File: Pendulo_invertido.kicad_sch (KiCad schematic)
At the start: 9 parts, among them IC2 MPU-6050, J3 Conn_01x02, J4 Conn_01x02, J5 Conn_01x02, U1 ESP32-devkitc, U2 TB6612FNG, U3 LM7805_TO220

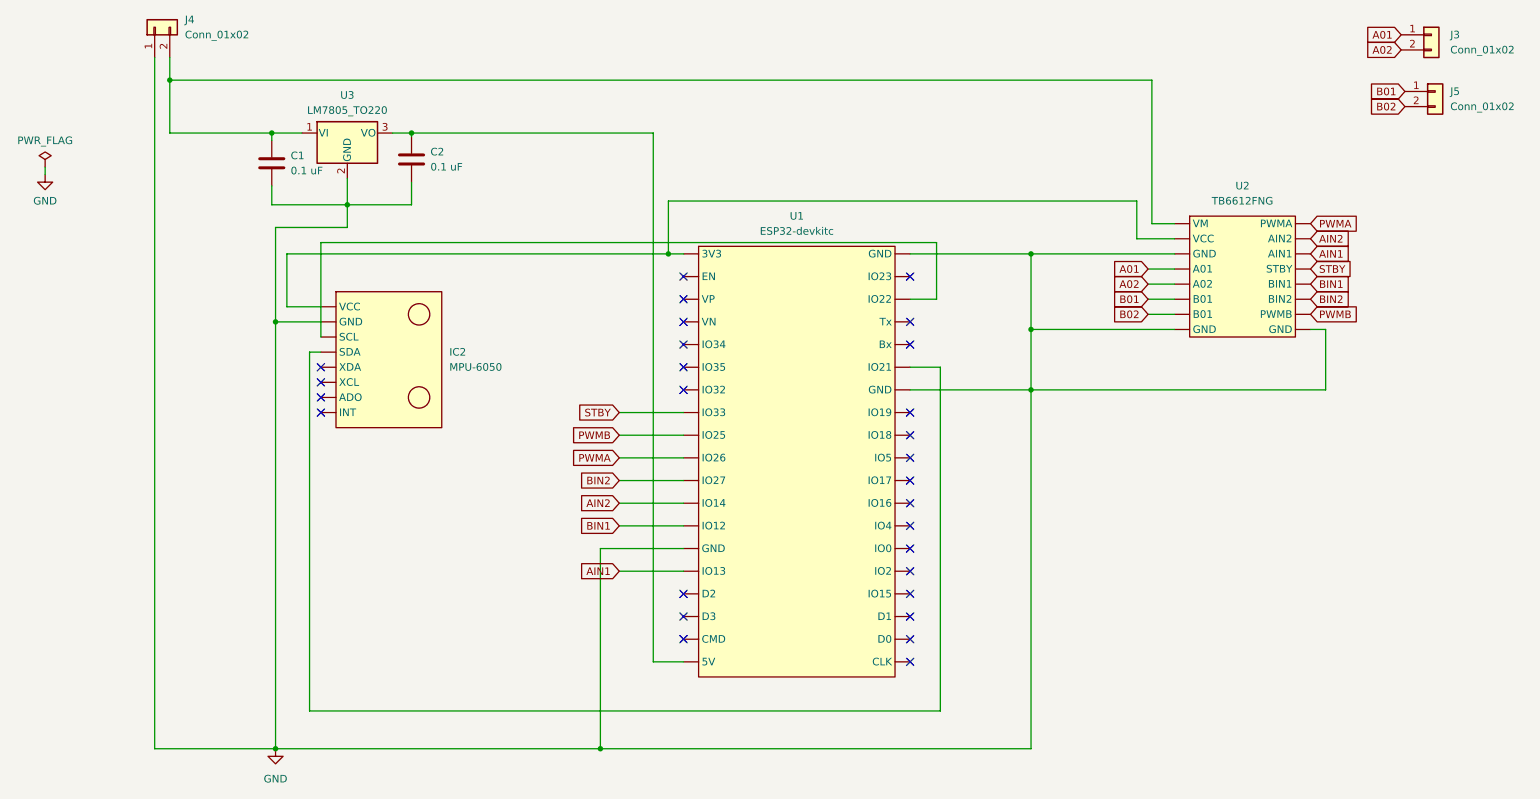
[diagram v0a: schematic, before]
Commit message: Creacion huellas esp32 y MPU
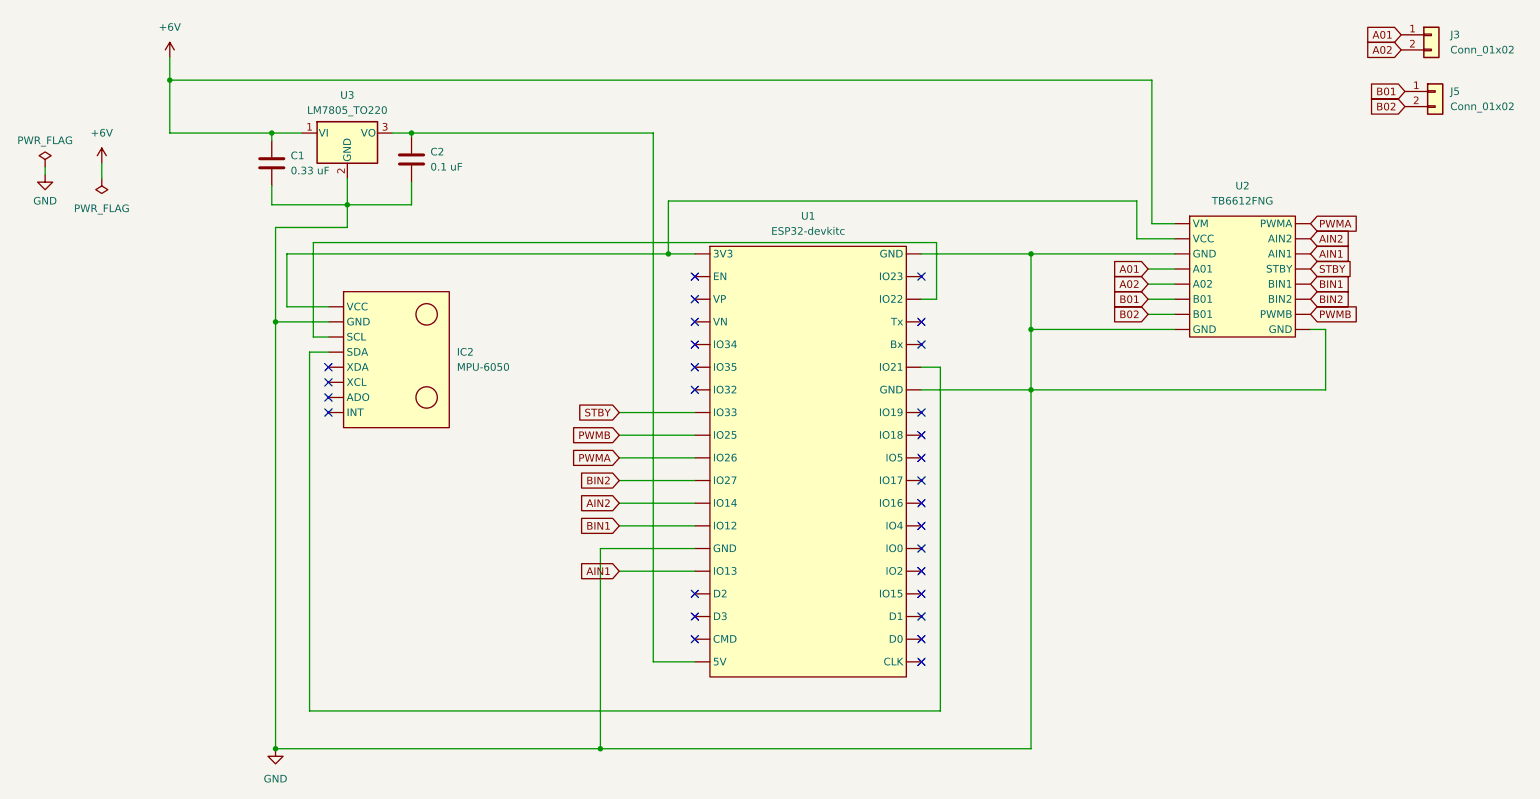
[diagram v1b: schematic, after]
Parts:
- removed J4: Conn_01x02, symbol Connector_Generic:Conn_01x02
- C1: value 0.1 uF -> 0.33 uF; footprint (none) -> Capacitor_THT:CP_Radial_D5.0mm_P2.00mm
- C2: footprint (none) -> Capacitor_THT:CP_Radial_D5.0mm_P2.00mm
- J3, J5: footprint (none) -> Connector_JST:JST_XH_B2B-XH-A_1x02_P2.50mm_Vertical
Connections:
- net +6V: now reaches C1.1, U2. (VM), U3.1 (VI)
- new net: IC2. (XDA), U1. (VP), U2. (VM)
- new net: IC2. (XDA), U1. (VP) (x2)
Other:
- moved on the sheet: IC2

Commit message: Creación pcb
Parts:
- removed IC2: MPU-6050, symbol New_Library:MPU-6050
- added IC1: MPU-6050, symbol New_Library:MPU-6050
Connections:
- net +6V: now also U2.1 (VM); no longer U2. (VM)
- net A01: now also U2.4 (A01); no longer U2. (VM)
- net A02: now also U2.5 (A02); no longer U2. (VM)
- net AIN1: now also U1.15 (IO13), U2.14 (AIN1); no longer U1. (VP), U2. (VM)
- net AIN2: now also U1.12 (IO14), U2.15 (AIN2); no longer U1. (VP), U2. (VM)
- net B01: now also U2.6 (B01); no longer U2. (VM)
- net B02: now also U2.7 (B01); no longer U2. (VM)
- net BIN1: now also U1.13 (IO12), U2.12 (BIN1); no longer U1. (VP), U2. (VM)
- net BIN2: now also U1.11 (IO27), U2.11 (BIN2); no longer U1. (VP), U2. (VM)
- net GND: now also U1.14 (GND), U1.32 (GND), U1.38 (GND), U2.3 (GND), U2.8 (GND), U2.9 (GND), IC1.2 (GND); no longer U1. (VP), U2. (VM)
- net PWMA: now also U1.10 (IO26), U2.16 (PWMA); no longer U1. (VP), U2. (VM)
- net PWMB: now also U1.9 (IO25), U2.10 (PWMB); no longer U1. (VP), U2. (VM)
- net STBY: now also U1.8 (IO33), U2.13 (STBY); no longer U1. (VP), U2. (VM)
- net at C2.1, U3.3 (VO): now also U1.19 (5V); no longer U1. (VP)
- new net: IC1.1 (VCC), U1.1 (3V3), U2.2 (VCC)
- new net: IC1.4 (SDA), U1.33 (IO21)
- new net: IC1.3 (SCL), U1.36 (IO22)

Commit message: Cambios huellas y pcb
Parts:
- added J1: Conn_01x02, TerminalBlock_Phoenix:TerminalBlock_Phoenix_MKDS-1,5-2-5.08_1x02_P5.08mm_Horizontal, symbol Connector_Generic:Conn_01x02
- IC1: footprint (none) -> Library:MPU6050
- J3, J5: footprint Connector_JST:JST_XH_B2B-XH-A_1x02_P2.50mm_Vertical -> TerminalBlock_Phoenix:TerminalBlock_Phoenix_MKDS-1,5-2-5.08_1x02_P5.08mm_Horizontal
- U1: footprint (none) -> Library:ESP32-devkitc-v4
- U2: footprint (none) -> Library:TB6612FNG
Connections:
- net +6V: now also J1.2 (Pin_2)
- net GND: now also J1.1 (Pin_1)
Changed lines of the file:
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@@
 (kicad_sch (version 20230121) (generator eeschema)
   (paper "A4")
+  (junction (at 49.53 36.83) (diameter 0) (color 0 0 0 0)
+  )
   (junction (at 66.675 45.72) (diameter 0) (color 0 0 0 0)
   )
+  (junction (at 49.53 33.02) (diameter 0) (color 0 0 0 0)
+  )
   (junction (at 133.35 66.04) (diameter 0) (color 0 0 0 0)
   )
   (junction (at 67.31 77.47) (diameter 0) (color 0 0 0 0)
-  )
-  (junction (at 49.53 36.83) (diameter 0) (color 0 0 0 0)
   )
   (junction (at 79.375 57.785) (diameter 0) (color 0 0 0 0)
@@
   (no_connect (at 177.165 130.81))
   (no_connect (at 177.165 104.14))
+  (wire (pts (xy 46.99 33.02) (xy 46.99 149.225))
+    (stroke (width 0) (type default))
+  )
   (wire (pts (xy 243.84 88.9) (xy 194.31 88.9))
     (stroke (width 0) (type default))
@@
     (stroke (width 0) (type default))
   )
+  (wire (pts (xy 67.945 33.02) (xy 67.945 32.385))
+    (stroke (width 0) (type default))
+  )
   (wire (pts (xy 213.995 76.2) (xy 218.44 76.2))
     (stroke (width 0) (type default))
@@
     (stroke (width 0) (type default))
   )
+  (wire (pts (xy 46.99 149.225) (xy 67.31 149.225))
+    (stroke (width 0) (type default))
+  )
   (wire (pts (xy 194.31 149.225) (xy 121.92 149.225))
     (stroke (width 0) (type default))
@@
     (stroke (width 0) (type default))
   )
+  (wire (pts (xy 49.53 33.02) (xy 67.945 33.02))
+    (stroke (width 0) (type default))
+  )
   (wire (pts (xy 177.165 88.9) (xy 194.31 88.9))
     (stroke (width 0) (type default))
@@
     (stroke (width 0) (type default))
   )
+  (wire (pts (xy 49.53 33.02) (xy 49.53 36.83))
+    (stroke (width 0) (type default))
+  )
   (wire (pts (xy 73.025 142.875) (xy 73.025 82.55))
     (stroke (width 0) (type default))
@@
   )
   (wire (pts (xy 212.09 63.5) (xy 212.09 57.15))
-    (stroke (width 0) (type default))
-  )
-  (wire (pts (xy 49.53 33.02) (xy 49.53 36.83))
     (stroke (width 0) (type default))
   )
@@
       (effects (font (size 1.27 1.27)))
     )
-    (property "Footprint" "" (at 146.685 64.77 0)
+    (property "Footprint" "Library:ESP32-devkitc-v4" (at 146.685 64.77 0)
       (effects (font (size 1.27 1.27)) hide)
     )
@@
       (effects (font (size 1.27 1.27)) (justify left))
     )
-    (property "Footprint" "Connector_JST:JST_XH_B2B-XH-A_1x02_P2.50mm_Vertical" (at 261.62 29.21 0)
+    (property "Footprint" "TerminalBlock_Phoenix:TerminalBlock_Phoenix_MKDS-1,5-2-5.08_1x02_P5.08mm_Horizontal" (at 261.62 29.21 0)
       (effects (font (size 1.27 1.27)) hide)
     )
@@
       (effects (font (size 1.27 1.27)))
     )
-    (property "Footprint" "" (at 226.06 58.42 0)
+    (property "Footprint" "Library:TB6612FNG" (at 226.06 58.42 0)
       (effects (font (size 1.27 1.27)) hide)
     )
@@
     )
   )
+  (symbol (lib_id "Connector_Generic:Conn_01x02") (at 46.99 27.94 90) (unit 1)
+    (in_bom yes) (on_board yes) (dnp no) (fields_autoplaced)
+    (property "Reference" "J1" (at 52.07 26.67 90)
+      (effects (font (size 1.27 1.27)) (justify right))
+    )
+    (property "Value" "Conn_01x02" (at 52.07 29.21 90)
+      (effects (font (size 1.27 1.27)) (justify right))
+    )
+    (property "Footprint" "TerminalBlock_Phoenix:TerminalBlock_Phoenix_MKDS-1,5-2-5.08_1x02_P5.08mm_Horizontal" (at 46.99 27.94 0)
+      (effects (font (size 1.27 1.27)) hide)
+    )
+    (property "Datasheet" "~" (at 46.99 27.94 0)
+      (effects (font (size 1.27 1.27)) hide)
+    )
+    (pin "1")
+    (pin "2")
+    (instances
+      (project "Pendulo_invertido"
+        (path "/1d6a1010-cae9-4f43-acf9-dddad0fedfc5"
+          (reference "J1") (unit 1)
+        )
+      )
+    )
+  )
   (symbol (lib_id "power:PWR_FLAG") (at 38.1 53.34 180) (unit 1)
     (in_bom yes) (on_board yes) (dnp no) (fields_autoplaced)
@@
     )
   )
-  (symbol (lib_id "power:+6V") (at 49.53 33.02 0) (unit 1)
-    (in_bom yes) (on_board yes) (dnp no) (fields_autoplaced)
-    (property "Reference" "#PWR03" (at 49.53 36.83 0)
-      (effects (font (size 1.27 1.27)) hide)
-    )
-    (property "Value" "+6V" (at 49.53 27.94 0)
-      (effects (font (size 1.27 1.27)))
-    )
-    (property "Footprint" "" (at 49.53 33.02 0)
-      (effects (font (size 1.27 1.27)) hide)
-    )
-    (property "Datasheet" "" (at 49.53 33.02 0)
+  (symbol (lib_id "power:GND") (at 28.575 52.705 0) (unit 1)
+    (in_bom yes) (on_board yes) (dnp no) (fields_autoplaced)
+    (property "Reference" "#PWR02" (at 28.575 59.055 0)
+      (effects (font (size 1.27 1.27)) hide)
+    )
+    (property "Value" "GND" (at 28.575 57.15 0)
+      (effects (font (size 1.27 1.27)))
+    )
+    (property "Footprint" "" (at 28.575 52.705 0)
+      (effects (font (size 1.27 1.27)) hide)
+    )
+    (property "Datasheet" "" (at 28.575 52.705 0)
+      (effects (font (size 1.27 1.27)) hide)
+    )
+    (pin "1")
+    (instances
+      (project "Pendulo_invertido"
+        (path "/1d6a1010-cae9-4f43-acf9-dddad0fedfc5"
+          (reference "#PWR02") (unit 1)
+        )
+      )
+    )
+  )
+  (symbol (lib_id "Connector_Generic:Conn_01x02") (at 262.255 38.735 0) (unit 1)
+    (in_bom yes) (on_board yes) (dnp no) (fields_autoplaced)
+    (property "Reference" "J5" (at 264.795 38.735 0)
+      (effects (font (size 1.27 1.27)) (justify left))
+    )
+    (property "Value" "Conn_01x02" (at 264.795 41.275 0)
+      (effects (font (size 1.27 1.27)) (justify left))
+    )
+    (property "Footprint" "TerminalBlock_Phoenix:TerminalBlock_Phoenix_MKDS-1,5-2-5.08_1x02_P5.08mm_Horizontal" (at 262.255 38.735 0)
+      (effects (font (size 1.27 1.27)) hide)
+    )
+    (property "Datasheet" "~" (at 262.255 38.735 0)
+      (effects (font (size 1.27 1.27)) hide)
+    )
+    (pin "1")
+    (pin "2")
+    (instances
+      (project "Pendulo_invertido"
+        (path "/1d6a1010-cae9-4f43-acf9-dddad0fedfc5"
+          (reference "J5") (unit 1)
+        )
+      )
+    )
+  )
+  (symbol (lib_id "Device:C") (at 90.17 50.165 0) (unit 1)
+    (in_bom yes) (on_board yes) (dnp no) (fields_autoplaced)
+    (property "Reference" "C2" (at 93.345 48.895 0)
+      (effects (font (size 1.27 1.27)) (justify left))
+    )
+    (property "Value" "0.1 uF" (at 93.345 51.435 0)
+      (effects (font (size 1.27 1.27)) (justify left))
+    )
+    (property "Footprint" "Capacitor_THT:CP_Radial_D5.0mm_P2.00mm" (at 91.1352 53.975 0)
+      (effects (font (size 1.27 1.27)) hide)
+    )
+    (property "Datasheet" "~" (at 90.17 50.165 0)
+      (effects (font (size 1.27 1.27)) hide)
+    )
+    (pin "1")
+    (pin "2")
+    (instances
+      (project "Pendulo_invertido"
+        (path "/1d6a1010-cae9-4f43-acf9-dddad0fedfc5"
+          (reference "C2") (unit 1)
+        )
+      )
+    )
+  )
+  (symbol (lib_id "power:+6V") (at 67.945 32.385 0) (unit 1)
+    (in_bom yes) (on_board yes) (dnp no) (fields_autoplaced)
+    (property "Reference" "#PWR03" (at 67.945 36.195 0)
+      (effects (font (size 1.27 1.27)) hide)
+    )
+    (property "Value" "+6V" (at 67.945 27.94 0)
+      (effects (font (size 1.27 1.27)))
+    )
+    (property "Footprint" "" (at 67.945 32.385 0)
+      (effects (font (size 1.27 1.27)) hide)
+    )
+    (property "Datasheet" "" (at 67.945 32.385 0)
       (effects (font (size 1.27 1.27)) hide)
     )
@@
     )
   )
-  (symbol (lib_id "power:GND") (at 28.575 52.705 0) (unit 1)
-    (in_bom yes) (on_board yes) (dnp no) (fields_autoplaced)
-    (property "Reference" "#PWR02" (at 28.575 59.055 0)
-      (effects (font (size 1.27 1.27)) hide)
-    )
-    (property "Value" "GND" (at 28.575 57.15 0)
-      (effects (font (size 1.27 1.27)))
-    )
-    (property "Footprint" "" (at 28.575 52.705 0)
-      (effects (font (size 1.27 1.27)) hide)
-    )
-    (property "Datasheet" "" (at 28.575 52.705 0)
-      (effects (font (size 1.27 1.27)) hide)
-    )
-    (pin "1")
-    (instances
-      (project "Pendulo_invertido"
-        (path "/1d6a1010-cae9-4f43-acf9-dddad0fedfc5"
-          (reference "#PWR02") (unit 1)
-        )
-      )
-    )
-  )
-  (symbol (lib_id "Connector_Generic:Conn_01x02") (at 262.255 38.735 0) (unit 1)
-    (in_bom yes) (on_board yes) (dnp no) (fields_autoplaced)
-    (property "Reference" "J5" (at 264.795 38.735 0)
-      (effects (font (size 1.27 1.27)) (justify left))
-    )
-    (property "Value" "Conn_01x02" (at 264.795 41.275 0)
-      (effects (font (size 1.27 1.27)) (justify left))
-    )
-    (property "Footprint" "Connector_JST:JST_XH_B2B-XH-A_1x02_P2.50mm_Vertical" (at 262.255 38.735 0)
-      (effects (font (size 1.27 1.27)) hide)
-    )
-    (property "Datasheet" "~" (at 262.255 38.735 0)
-      (effects (font (size 1.27 1.27)) hide)
-    )
-    (pin "1")
-    (pin "2")
-    (instances
-      (project "Pendulo_invertido"
-        (path "/1d6a1010-cae9-4f43-acf9-dddad0fedfc5"
-          (reference "J5") (unit 1)
-        )
-      )
-    )
-  )
-  (symbol (lib_id "Device:C") (at 90.17 50.165 0) (unit 1)
-    (in_bom yes) (on_board yes) (dnp no) (fields_autoplaced)
-    (property "Reference" "C2" (at 93.345 48.895 0)
-      (effects (font (size 1.27 1.27)) (justify left))
-    )
-    (property "Value" "0.1 uF" (at 93.345 51.435 0)
-      (effects (font (size 1.27 1.27)) (justify left))
-    )
-    (property "Footprint" "Capacitor_THT:CP_Radial_D5.0mm_P2.00mm" (at 91.1352 53.975 0)
-      (effects (font (size 1.27 1.27)) hide)
-    )
-    (property "Datasheet" "~" (at 90.17 50.165 0)
-      (effects (font (size 1.27 1.27)) hide)
-    )
-    (pin "1")
-    (pin "2")
-    (instances
-      (project "Pendulo_invertido"
-        (path "/1d6a1010-cae9-4f43-acf9-dddad0fedfc5"
-          (reference "C2") (unit 1)
-        )
-      )
-    )
-  )
   (symbol (lib_id "power:GND") (at 67.31 149.225 0) (unit 1)
     (in_bom yes) (on_board yes) (dnp no) (fields_autoplaced)
@@
       (effects (font (size 1.27 1.27)) (justify left))
     )
-    (property "Footprint" "" (at 83.185 71.12 0)
-      (effects (font (size 1.27 1.27)) hide)
-    )
+    (property "Footprint" "Library:MPU6050" (at 83.185 71.12 0)
+      (effects (font (size 1.27 1.27)) hide)
+    )
